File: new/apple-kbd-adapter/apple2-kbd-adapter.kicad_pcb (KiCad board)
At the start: 2 copper layers, 35.8 x 45.7 mm, 8 parts, among them J1 Keyboard, J2 ~RESET, J3 ~CLEAR_SCREEN, J4 Apple 1, SW1 SW_SPST, SW2 SW_SPST

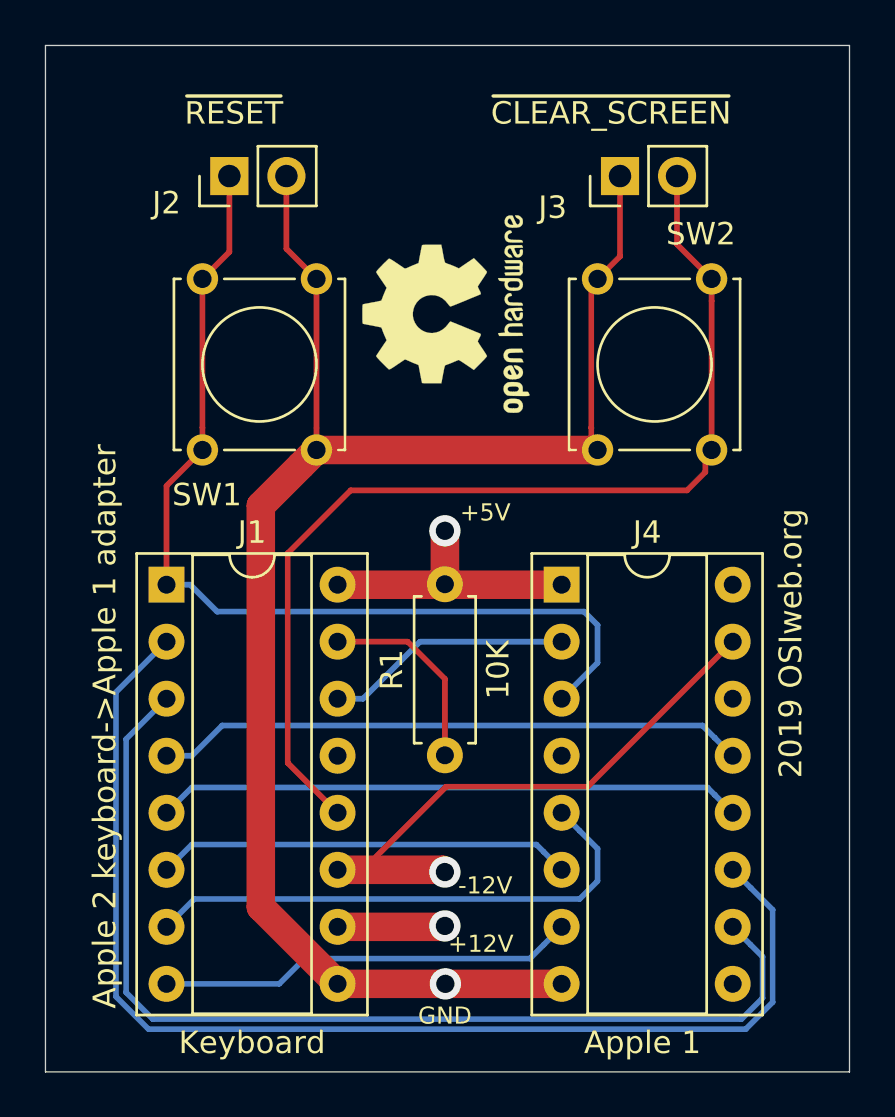
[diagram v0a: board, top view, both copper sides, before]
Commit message: - fixed mislabeled keyboard and apple connectors - swapped position of keyboard and apple connectors to be able to use same-side cables
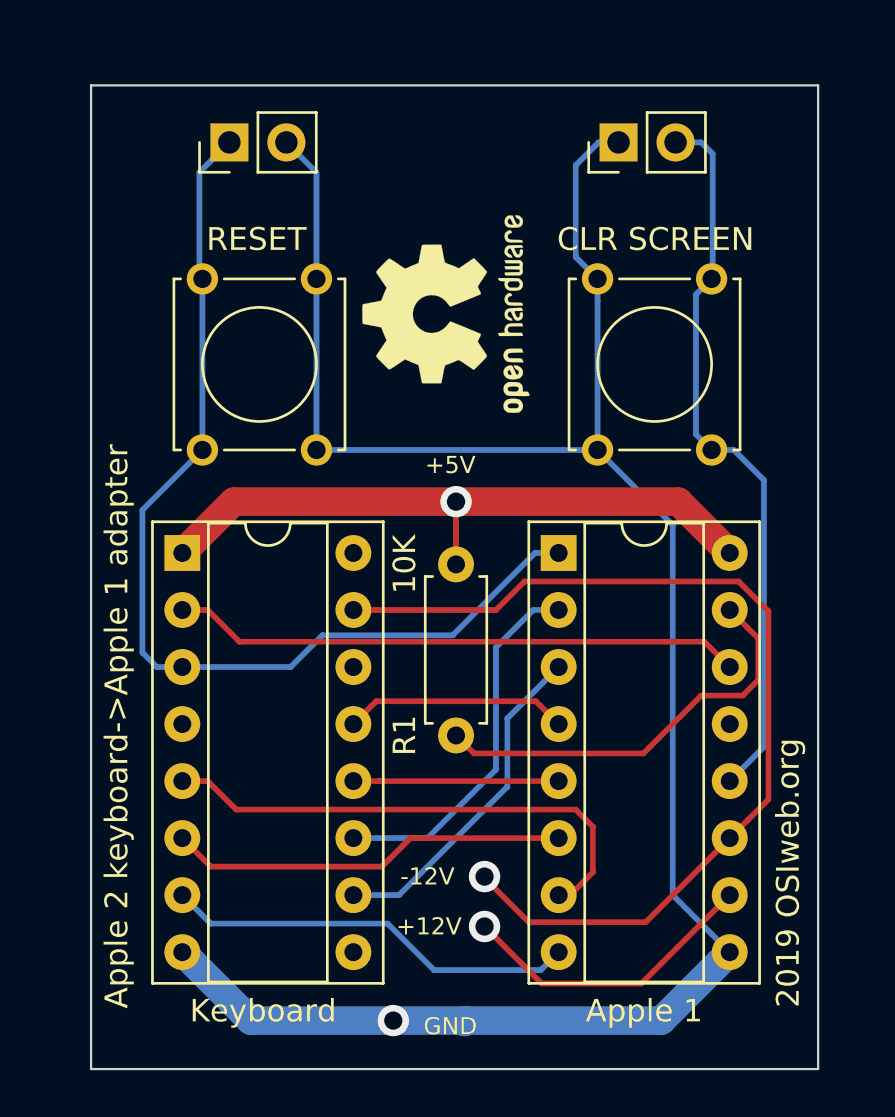
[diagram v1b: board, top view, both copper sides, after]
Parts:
- J1: value Keyboard -> Apple 1
- J4: value Apple 1 -> Keyboard
- moved J1 17.5 mm to (112.3, 81.8)
- moved J4 17.0 mm to (95.5, 81.8)
- moved J3 1.50 mm to (114.9, 63.5)
- moved J2 1.50 mm to (97.6, 63.5)
- moved R1 1.01 mm to (107.7, 89.9)
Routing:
- net /D4: track 53.7 -> 16.5 mm
- net /D3: track 46.8 -> 15.1 mm
- net /GND: track 73.8 -> 94.0 mm
- net /-12V: track 26.6 -> 43.9 mm
- net /D1: track 26.2 -> 9.14 mm
- net /+5V: track 12.4 -> 29.1 mm
- net /D2: track 26.3 -> 9.99 mm
- net /~STROBE: track 11.0 -> 25.4 mm
- net /~CLRSCR: track 46.4 -> 32.6 mm
- net /D8: track 8.87 -> 18.8 mm
- net /+12V: track 4.80 -> 13.6 mm
- net /~RESET: track 43.2 -> 45.4 mm
- net /D5: track 18.5 -> 17.8 mm
- net /D6: track 23.7 -> 23.1 mm
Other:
- board size 35.8 x 45.7 mm -> 32.4 x 43.8 mm
- board text added: "CLR SCREEN"
- board text added: "RESET"

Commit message: Fixed CLEAR miswiring
- (FIXED) The CLEAR button was wired to GROUND instead of +5V.
- Added rev number to PCB and added design info to design sheets
- Added no-connect symobols to unconnected pins on schematic
- Added a README file.
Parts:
- R1: value 10K -> 3.3k
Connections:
- net /+12V renamed Net-(J1-Pad10)
- J2 pad 1: /~RESET -> /GND
- J2 pad 2: /GND -> /~RESET
- J3 pad 1: /GND -> /+5V
- SW1 pad 1: /~RESET -> /GND
- SW1 pad 2: /GND -> /~RESET
- SW2 pad 1: /GND -> /+5V
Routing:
- net /GND: track 94.0 -> 66.6 mm
- net /+5V: track 29.1 -> 46.8 mm
- net /~RESET: track 45.4 -> 42.5 mm
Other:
- board text added: "Apple 2 keyboard->Apple 1 adapter rev 1.1"
- board text removed: "7/30/2019"
- board text removed: "Apple 2 keyboard->Apple 1 adapter"
